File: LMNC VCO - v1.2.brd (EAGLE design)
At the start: 27.9 x 110.5 mm, 51 parts, among them IC1 CEM3340, J1 JACKS, J10 LINK, P1 POWER, U1 TL072CP, U2 TL074CN

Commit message: Started Layout
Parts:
- removed U$1: (no value), eurohelper:EURO_PCB_6HP
- added J2, J3, J4, J5, J6, J7, J8: PJ301_THONKICONNTME, og-pj301:WQP_PJ_301M_TME
- added R16: 10kB, parts_aman:ALPS_POT_VERTICAL
- J1: value JACKS -> PJ301_THONKICONNTME; device con-headers-jp:SIP-100-10-32Y -> og-pj301:WQP_PJ_301M_TME
- moved RV4 150.4 mm to (148.0, 101.6)
- moved RV2 150.1 mm to (134.0, 101.6)
- moved RV5 123.3 mm to (148.0, 117.5)
- moved J1 116.5 mm to (131.4, 60.3), flipped to the bottom, turned to 180 degrees
- moved RV7 108.8 mm to (134.0, 133.3)
- moved U$2 41.2 mm to (125.7, 20.3)
- moved RV6 20.7 mm to (87.0, 75.6)
- moved RV8 7.10 mm to (62.2, 67.9)
- moved C1 6.54 mm to (45.1, 54.0)
- moved R20 5.46 mm to (81.9, 27.3)
- moved R41 1.27 mm to (15.9, 30.2)
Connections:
- net 1VOCTIN: no longer J1.9
- net CVIN: no longer J1.8
- net FMINPUT: no longer J1.4
- net GND: no longer J1.1, J1.10
- net PWMIN: no longer J1.2
- net RAMPOUT: no longer J1.7
- net SQUAREOUT: no longer J1.3
- net SYNCIN1: no longer J1.6
- net TRIANGLEOUT: no longer J1.5
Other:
- board text added: "1OIN"
- board text added: "CVIN"
- board text added: "FMIN"
- board text added: "PWIN"
- board text added: "ROUT"
- board text added: "SOUT"
- board text added: "SYIN"
- board text added: "TOUT"

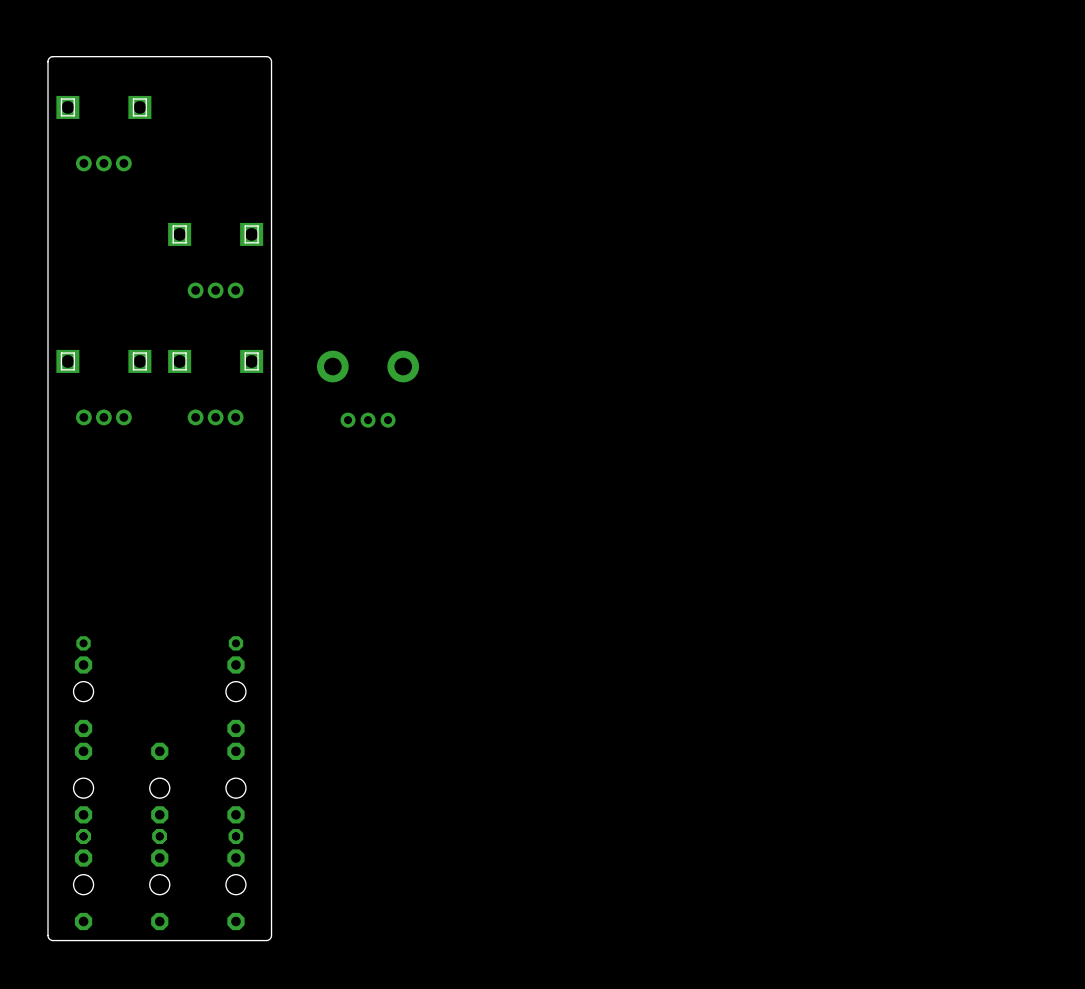
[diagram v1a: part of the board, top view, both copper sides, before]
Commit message: Started two layered pcb design
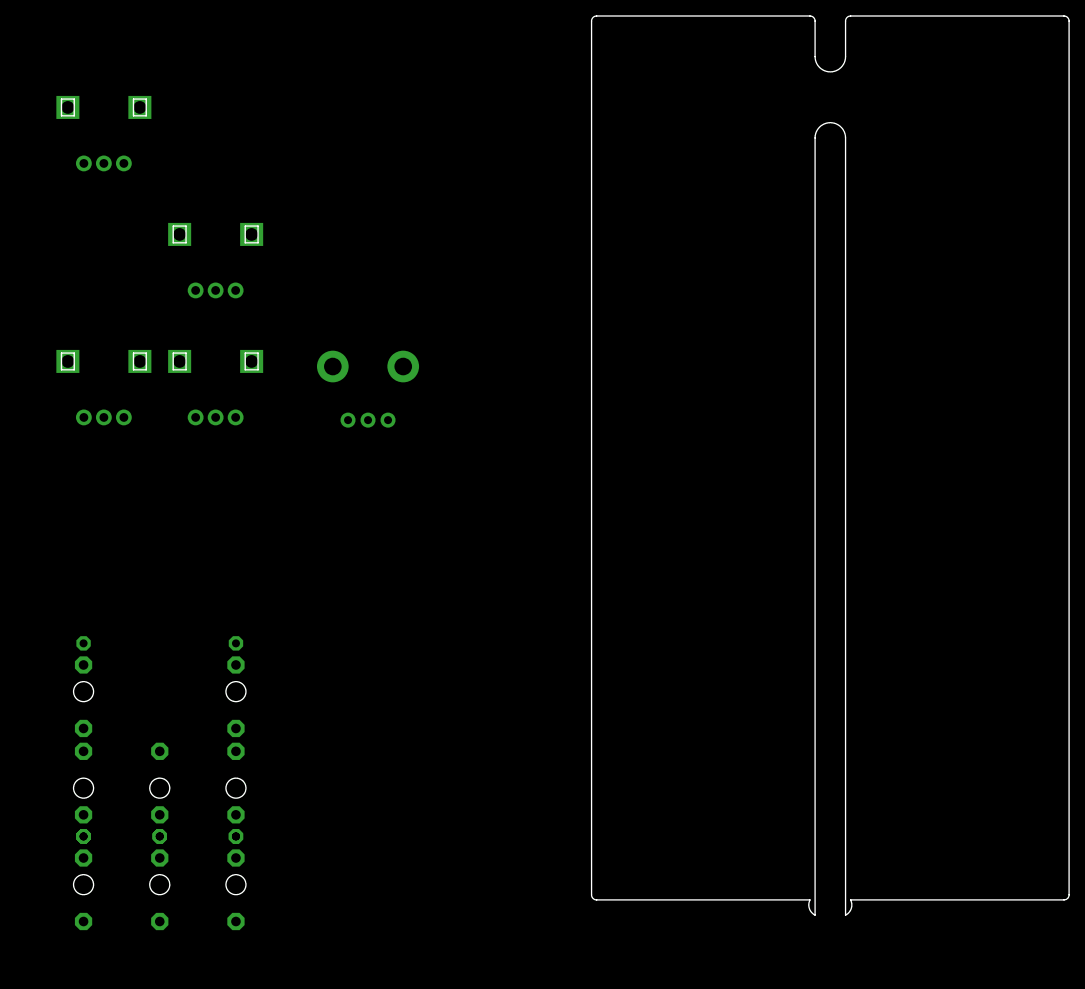
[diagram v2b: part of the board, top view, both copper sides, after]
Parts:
- removed U$2: (no value), eurohelper:EURO_PCB_6HP
- added U$1: (no value), eurohelper1:EURO_PCB_6HP
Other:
- board size 27.9 x 110.5 mm -> 59.7 x 112.4 mm
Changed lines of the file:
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@@
 <drawing>
 <settings>
-<setting alwaysvectorfont="no"/>
+<setting alwaysvectorfont="yes"/>
 <setting verticaltext="up"/>
 </settings>
@@
 <attribute name="VALUE" x="51.816" y="53.848" size="1.27" layer="27" ratio="10" rot="R180"/>
 </element>
-<element name="U$2" library="eurohelper" package="EURO_PCB_6HP" value="" x="125.73" y="20.32" smashed="yes"/>
 <element name="R16" library="parts_aman" package="ALPS_POT_VERTICAL" value="10kB" x="167.005" y="100.965" smashed="yes" rot="MR0">
 <attribute name="NAME" x="167.005" y="107.95" size="1.27" layer="26" font="vector" ratio="16" rot="MR0" align="center"/>
@@
 <attribute name="NAME" x="154.36" y="30.4" size="1.27" layer="26" rot="MR0"/>
 </element>
+<element name="U$1" library="eurohelper1" package="EURO_PCB_6HP" value="" x="193.675" y="25.4" smashed="yes"/>
 </elements>
 <signals>

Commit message: up
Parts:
- removed R16: 10kB, parts_aman:ALPS_POT_VERTICAL
- RV2: value 100K PWMLVL -> 100kB PWMLVL; device pot:EVUF -> parts_aman:ALPS_POT_VERTICAL
- RV4: value 100K PW -> 100kB PW; device pot:EVUF -> parts_aman:ALPS_POT_VERTICAL
- RV5: value 100K CV LVL -> 100kB CVLVL; device pot:EVUF -> parts_aman:ALPS_POT_VERTICAL
- RV7: value 100K FINETUNE -> 100kB FINETUNE; device pot:EVUF -> parts_aman:ALPS_POT_VERTICAL
- moved U$1 8.52 mm to (201.3, 21.6)
- moved RV4 0.64 mm to (147.3, 101.6)
- moved RV5 0.64 mm to (147.3, 117.5)
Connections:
- net CVIN: now also RV5.3; no longer RV5.1
- net GND: now also RV5.1; no longer RV5.3
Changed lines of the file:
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@@
 <drawing>
 <settings>
-<setting alwaysvectorfont="yes"/>
+<setting alwaysvectorfont="no"/>
 <setting verticaltext="up"/>
 </settings>
@@
 <attribute name="VALUE" x="53.975" y="61.2775" size="1.27" layer="28" ratio="12" rot="MR90"/>
 </element>
-<element name="RV2" library="pot" library_urn="urn:adsk.eagle:library:331" package="EVUF" package3d_urn="urn:adsk.eagle:package:22730/1" value="100K PWMLVL" x="133.985" y="101.6" smashed="yes" rot="MR0">
-<attribute name="NAME" x="128.9375" y="99.52" size="1.27" layer="26" rot="MR270"/>
-<attribute name="POPULARITY" value="0" x="95.885" y="63.5" size="1.778" layer="28" rot="MR0" display="off"/>
-<attribute name="VALUE" x="138.485" y="92.1" size="1.27" layer="28" rot="MR0"/>
-</element>
-<element name="RV4" library="pot" library_urn="urn:adsk.eagle:library:331" package="EVUF" package3d_urn="urn:adsk.eagle:package:22730/1" value="100K PW" x="147.955" y="101.6" smashed="yes" rot="MR0">
-<attribute name="NAME" x="142.9075" y="99.52" size="1.27" layer="26" rot="MR270"/>
-<attribute name="POPULARITY" value="0" x="83.185" y="63.5" size="1.778" layer="28" rot="MR0" display="off"/>
-<attribute name="VALUE" x="152.455" y="92.1" size="1.27" layer="28" rot="MR0"/>
-</element>
-<element name="RV5" library="pot" library_urn="urn:adsk.eagle:library:331" package="EVUF" package3d_urn="urn:adsk.eagle:package:22730/1" value="100K CV LVL" x="147.955" y="117.475" smashed="yes" rot="MR0">
-<attribute name="NAME" x="142.9075" y="115.395" size="1.27" layer="26" rot="MR270"/>
-<attribute name="POPULARITY" value="0" x="95.885" y="79.375" size="1.778" layer="28" rot="MR0" display="off"/>
-<attribute name="VALUE" x="152.455" y="107.975" size="1.27" layer="28" rot="MR0"/>
-</element>
 <element name="RV6" library="bourns" package="3386W" value="100K CENTER NOTE" x="86.995" y="75.565" smashed="yes" rot="MR90">
 <attribute name="NAME" x="88.9" y="69.215" size="1.27" layer="26" ratio="12" rot="MR0"/>
 <attribute name="VALUE" x="90.17" y="72.0725" size="1.27" layer="28" ratio="12" rot="MR90"/>
 </element>
-<element name="RV7" library="pot" library_urn="urn:adsk.eagle:library:331" package="EVUF" package3d_urn="urn:adsk.eagle:package:22730/1" value="100K FINETUNE" x="133.985" y="133.35" smashed="yes" rot="MR0">
-<attribute name="NAME" x="127.6025" y="128.1275" size="1.27" layer="26" rot="MR90"/>
-<attribute name="POPULARITY" value="0" x="111.125" y="95.25" size="1.778" layer="28" rot="MR0" display="off"/>
-<attribute name="VALUE" x="138.485" y="123.85" size="1.27" layer="28" rot="MR0"/>
-</element>
 <element name="RV8" library="bourns" package="3386W" value="20K HF TRACK" x="62.23" y="67.945" smashed="yes" rot="MR90">
 <attribute name="NAME" x="65.405" y="68.8975" size="1.27" layer="26" ratio="12" rot="MR90"/>
@@
 <attribute name="VALUE" x="51.816" y="53.848" size="1.27" layer="27" ratio="10" rot="R180"/>
 </element>
-<element name="R16" library="parts_aman" package="ALPS_POT_VERTICAL" value="10kB" x="167.005" y="100.965" smashed="yes" rot="MR0">
-<attribute name="NAME" x="167.005" y="107.95" size="1.27" layer="26" font="vector" ratio="16" rot="MR0" align="center"/>
+<element name="RV2" library="parts_aman" package="ALPS_POT_VERTICAL" value="100kB PWMLVL" x="133.985" y="101.6" smashed="yes" rot="MR0">
+<attribute name="NAME" x="133.985" y="106.045" size="1.27" layer="26" font="vector" ratio="16" rot="MR0" align="center"/>
 </element>
 <element name="J1" library="og-pj301" package="WQP_PJ_301M_TME" value="PJ301_THONKICONNTME" x="131.445" y="60.325" smashed="yes" rot="MR180">
@@
 <attribute name="NAME" x="154.36" y="30.4" size="1.27" layer="26" rot="MR0"/>
 </element>
-<element name="U$1" library="eurohelper1" package="EURO_PCB_6HP" value="" x="193.675" y="25.4" smashed="yes"/>
+<element name="U$1" library="eurohelper1" package="EURO_PCB_6HP" value="" x="201.295" y="21.59" smashed="yes"/>
+<element name="RV4" library="parts_aman" package="ALPS_POT_VERTICAL" value="100kB PW" x="147.32" y="101.6" smashed="yes" rot="MR0">
+<attribute name="NAME" x="147.32" y="106.045" size="1.27" layer="26" font="vector" ratio="16" rot="MR0" align="center"/>
+</element>
+<element name="RV5" library="parts_aman" package="ALPS_POT_VERTICAL" value="100kB CVLVL" x="147.32" y="117.475" smashed="yes" rot="MR0">
+<attribute name="NAME" x="147.32" y="121.92" size="1.27" layer="26" font="vector" ratio="16" rot="MR0" align="center"/>
+</element>
+<element name="RV7" library="parts_aman" package="ALPS_POT_VERTICAL" value="100kB FINETUNE" x="133.985" y="133.35" smashed="yes" rot="MR0">
+<attribute name="NAME" x="133.985" y="137.795" size="1.27" layer="26" font="vector" ratio="16" rot="MR0" align="center"/>
+</element>
 </elements>
 <signals>
@@
 <contactref element="R15" pad="1"/>
 <contactref element="R10" pad="1"/>
-<contactref element="RV2" pad="1"/>
-<contactref element="RV7" pad="3"/>
 <contactref element="RV6" pad="1"/>
-<contactref element="RV5" pad="3"/>
 <contactref element="RV8" pad="3"/>
 <contactref element="C11" pad="2"/>
@@
 <contactref element="C5" pad="1"/>
 <contactref element="U2" pad="3"/>
-<wire x1="145.455" y1="110.475" x2="136.485" y2="94.6" width="0" layer="19" extent="1-1"/>
-<wire x1="131.485" y1="126.35" x2="145.455" y2="110.475" width="0" layer="19" extent="1-1"/>
-<wire x1="87.3125" y1="78.105" x2="136.485" y2="94.6" width="0" layer="19" extent="1-1"/>
+<contactref element="RV2" pad="1"/>
+<contactref element="RV5" pad="1"/>
+<contactref element="RV7" pad="3"/>
+<wire x1="149.82" y1="110.775" x2="136.485" y2="94.9" width="0" layer="19" extent="1-1"/>
+<wire x1="131.485" y1="126.65" x2="149.82" y2="110.775" width="0" layer="19" extent="1-1"/>
+<wire x1="87.3125" y1="78.105" x2="136.485" y2="94.9" width="0" layer="19" extent="1-1"/>
 <wire x1="62.5475" y1="65.405" x2="87.3125" y2="78.105" width="0" layer="19" extent="1-1"/>
 <wire x1="51.015" y1="50.8" x2="62.5475" y2="65.405" width="0" layer="19" extent="1-1"/>
@@
 <contactref element="R12" pad="1"/>
 <contactref element="RV4" pad="2"/>
-<wire x1="15.455" y1="27.305" x2="147.955" y2="94.6" width="0" layer="19" extent="1-1"/>
+<wire x1="15.455" y1="27.305" x2="147.32" y2="94.9" width="0" layer="19" extent="1-1"/>
 </signal>
 <signal name="N$14">
 <contactref element="R11" pad="1"/>
 <contactref element="RV2" pad="2"/>
-<wire x1="15.455" y1="24.4475" x2="133.985" y2="94.6" width="0" layer="19" extent="1-1"/>
+<wire x1="133.985" y1="94.9" x2="15.455" y2="24.4475" width="0" layer="19" extent="1-1"/>
 </signal>
 <signal name="N$15">
 <contactref element="R10" pad="2"/>
 <contactref element="RV4" pad="1"/>
-<wire x1="17.78" y1="38.52" x2="150.455" y2="94.6" width="0" layer="19" extent="1-1"/>
+<wire x1="17.78" y1="38.52" x2="149.82" y2="94.9" width="0" layer="19" extent="1-1"/>
 </signal>
 <signal name="N$16">
-<contactref element="RV4" pad="3"/>
 <contactref element="R13" pad="1"/>
-<wire x1="2.2225" y1="26.09125" x2="145.455" y2="94.6" width="0" layer="19" extent="1-1"/>
+<contactref element="RV4" pad="3"/>
+<wire x1="2.2225" y1="26.09125" x2="144.82" y2="94.9" width="0" layer="19" extent="1-1"/>
 </signal>
 <signal name="PWMIN">
-<contactref element="RV2" pad="3"/>
 <contactref element="J10" pad="5"/>
 <contactref element="J10" pad="6"/>
-<wire x1="69.215" y1="15.875" x2="131.485" y2="94.6" width="0" layer="19" extent="1-1"/>
+<contactref element="RV2" pad="3"/>
 <wire x1="69.215" y1="13.335" x2="69.215" y2="15.875" width="0" layer="19" extent="1-1"/>
+<wire x1="131.485" y1="94.9" x2="69.215" y2="15.875" width="0" layer="19" extent="1-1"/>
 </signal>
 <signal name="RAMPOUT">
@@
 <contactref element="RV7" pad="1"/>
 <wire x1="59.69" y1="13.335" x2="62.23" y2="13.335" width="0" layer="19" extent="1-1"/>
-<wire x1="136.485" y1="126.35" x2="62.23" y2="13.335" width="0" layer="19" extent="1-1"/>
+<wire x1="136.485" y1="126.65" x2="62.23" y2="13.335" width="0" layer="19" extent="1-1"/>
 </signal>
 <signal name="N$22">
 <contactref element="R24" pad="2"/>
 <contactref element="RV7" pad="2"/>
-<wire x1="133.985" y1="126.35" x2="76.62" y2="27.305" width="0" layer="19" extent="1-1"/>
+<wire x1="133.985" y1="126.65" x2="76.62" y2="27.305" width="0" layer="19" extent="1-1"/>
 </signal>
 <signal name="N$24">
@@
 <wire x1="50.38" y1="5.715" x2="69.215" y2="18.415" width="0" layer="19" extent="1-1"/>
 </signal>
-<signal name="CVIN">
-<contactref element="RV5" pad="1"/>
-</signal>
 <signal name="N$29">
 <contactref element="R20" pad="2"/>
 <contactref element="RV5" pad="2"/>
-<wire x1="147.955" y1="110.475" x2="82.765" y2="27.305" width="0" layer="19" extent="1-1"/>
+<wire x1="147.32" y1="110.775" x2="82.765" y2="27.305" width="0" layer="19" extent="1-1"/>
 </signal>
 <signal name="N$30">
@@
 <contactref element="U2" pad="5"/>
 </signal>
+<signal name="CVIN">
+<contactref element="RV5" pad="3"/>
+</signal>
 </signals>
